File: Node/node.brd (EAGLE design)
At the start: 76.2 x 33.9 mm, 121 parts, among them J1 U.FL, J2 USBSMD, J5 CORTEX_DEBUGPTH, SW2 SPST_TACT-KMR2, U1 MCP73871, U2 DW1000-I, U3 TPS61090RSAR, U4 ATSAMD21G-A, U5 LSM303C, U6 LM3880, X2 332-02, X3 32.768

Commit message: Part modifications, added part numbers to all parts (except resistors and capicators). Library consolidation.
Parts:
- B2: device microbuilder:JSTPH2 -> MainLib:JSTPH2
- C1, C2, C44: device microbuilder:0603-NO -> microbuilder:0603
- C18: value 1p2 -> 1.2pF
- C32: device SparkFun-Passives:0805 -> SparkFun-Capacitors:0603-CAP
- C33: value 100uF/6V - https://www.digikey.com/product-detail/en/avx-corporation/F930G107MBA/478-8135-1-ND/4005827 -> 100uF/6V
- C43: device microbuilder:0805-NO -> SparkFun-Passives:0805
- CHRG, DONE: device microbuilder:CHIPLED_0805_NOOUTLINE -> MainLib:CHIPLED_0805_NOOUTLINE
- D13: value RED -> ORANGE; device microbuilder:CHIPLED_0805_NOOUTLINE -> MainLib:CHIPLED_0805_NOOUTLINE
- J1: device adafruit:U.FL -> MainLib:U.FL
- J2: device SparkFun-Connectors:USB-MINIB -> MainLib:USB-MINIB
- L1, L2: device Wurth_Elektronik_Passive_rev15e:WE-CBA_0402(W=2.2) -> MainLib:WE-CBA_0402(W=2.2)
- L3: value NR8040T6R8N -> 6.8uH, 2A
- PWR, TXUART: value GREEN -> RED; device microbuilder:CHIPLED_0805_NOOUTLINE -> MainLib:CHIPLED_0805_NOOUTLINE
- R1, R2, R3: value 100 -> 470
- R32, R34: value 47K -> 10K
- RV1, RV2, RV3: value WE-VE_0603_REFLOW -> SUPPRESSOR-USB_0603_REFLOW; device Wurth_Elektronik_Passive_rev15e:WESURGE_0603_REFLOW -> MainLib:WESURGE_0603_REFLOW
- RX, RXOK, SFD, TX: device SparkFun-LED:LED-0603 -> MainLib:CHIPLED_0603_NOOUTLINE
- RXUART: value RED -> GREEN; device microbuilder:CHIPLED_0805_NOOUTLINE -> MainLib:CHIPLED_0805_NOOUTLINE
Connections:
- net VCC-ISO: now also R32.2
- net VLIPO: no longer R32.2
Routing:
- net VLIPO: track 12.2 -> 5.38 mm
- net VCC-ISO: track 45.8 -> 50.8 mm

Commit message: Resistor documentation
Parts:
- C1, C2, C44: device microbuilder:0603 -> SparkFun-Capacitors:0603-CAP
- C17, C22, C43, C6: device SparkFun-Passives:0805 -> SparkFun-Capacitors:0603-CAP
- R8, R9: value 10k -> 10K
- renumbered RXUART to UARTRX, TXUART to UARTTX

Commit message: Prep to move to a new power regulator, as previous one is only boost
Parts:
- added C36: 1uF, SparkFun-Capacitors:0603-CAP
- added SJ4, SJ5: (no value), jumper:SJ
- added U$12: 3.3V, MainLib:10-VFDFNEXPOSEDPAD
- R15, R16, R22: value 1K -> 470
- R28: value 68 -> 100K
- RT2: value 15K -> 10K
- renumbered THERM to RT2
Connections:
- new net N$19: C36.2, SJ4.1, U6.3
- net 3.3V: now also SJ4.2, SJ5.2; no longer U6.3
- net GND: now also C36.1
- net VDELAY: now also SJ5.1
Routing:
- net N$19: track 0.00 -> 10.7 mm, vias 0 -> 1
- net VDELAY: track 9.38 -> 14.8 mm, vias 0 -> 1
- net SDA: track 49.2 -> 53.3 mm
- net 3.3V: track 52.1 -> 50.1 mm, vias 26 -> 27
- net !CS_MAG: track 2.36 -> 3.33 mm
- net GND: vias 236 -> 237
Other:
- board text added: "Bubble if no C36"
- board text added: "Bubble if no U6"
- board text removed: "Accel / Compass"

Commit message: Initial pass of the new regulator circuit. Passes DRT.
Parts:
- removed R25: 205K, 1%, SparkFun-Resistors:0603-RES
- removed U3: TPS61090RSAR, microbuilder:PVQFN-16
- C30: value 2.2uF -> 15uF
- L3: value 6.8uH, 2A -> 3.3uH; device MainLib:IND_TAIYO_NR8040 -> MainLib:1212IND
- R24: value 1.15M, 1% -> 100
- moved U$12 12.8 mm to (54.9, 20.0), turned to 270 degrees
- moved L3 6.76 mm to (60.2, 23.4), turned to 90 degrees
- moved C30 6.20 mm to (60.2, 20.1)
- moved C32 5.05 mm to (54.6, 16.5)
- moved R24 3.21 mm to (51.8, 16.6), turned to 180 degrees
- moved C22 0.25 mm to (49.9, 20.3)
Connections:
- removed net N$20: L3.1, U3.3, U3.4
- new net N$29: L3.P1, U$12.PX2
- new net N$37: C32.1, R24.1, U$12.PX7, U$12.PX8
- net 3.3V: now also U$12.PX1, U$12.PX10; no longer R24.2, U3.1, U3.15, U3.16
- net GND: now also U$12.PAD@1, U$12.PX3, U$12.PX9; no longer R25.1, U3.10, U3.13, U3.5, U3.6, U3.7, U3.9, U3.P$18, U3.P$19, U3.P$20, U3.P$21, U3.P$22, U3.THERMAL
- net N$23: now also L3.P2, U$12.PX4; no longer R24.1, R25.2, U3.14
- net N$30: now also U$12.PX6; no longer U3.11
- net VCC-ISO: now also R24.2, U$12.PX5; no longer C32.1, L3.2, U3.8
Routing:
- net N$20: track 16.9 -> 0.00 mm
- net GND: track 8.49 -> 16.8 mm, vias 237 -> 249
- net N$23: track 4.88 -> 0.00 mm
- net VCC-ISO: track 50.9 -> 55.2 mm
- net N$37: track 0.00 -> 4.09 mm
- net N$30: track 57.7 -> 59.2 mm
- net !CS_MAG: track 3.33 -> 2.36 mm
- net 3.3V: track 50.1 -> 50.0 mm, vias 27 -> 26
- added copper zone on layer 1, net N$23
- added copper zone on layer 1, net N$29
- removed copper zone on layer 1, net N$20
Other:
- board text added: "ATSAMD21"
- board text added: "Charger"
- board text added: "Regulator"
- board text removed: "C32"
- board text removed: "R24"
- board text removed: "R25"

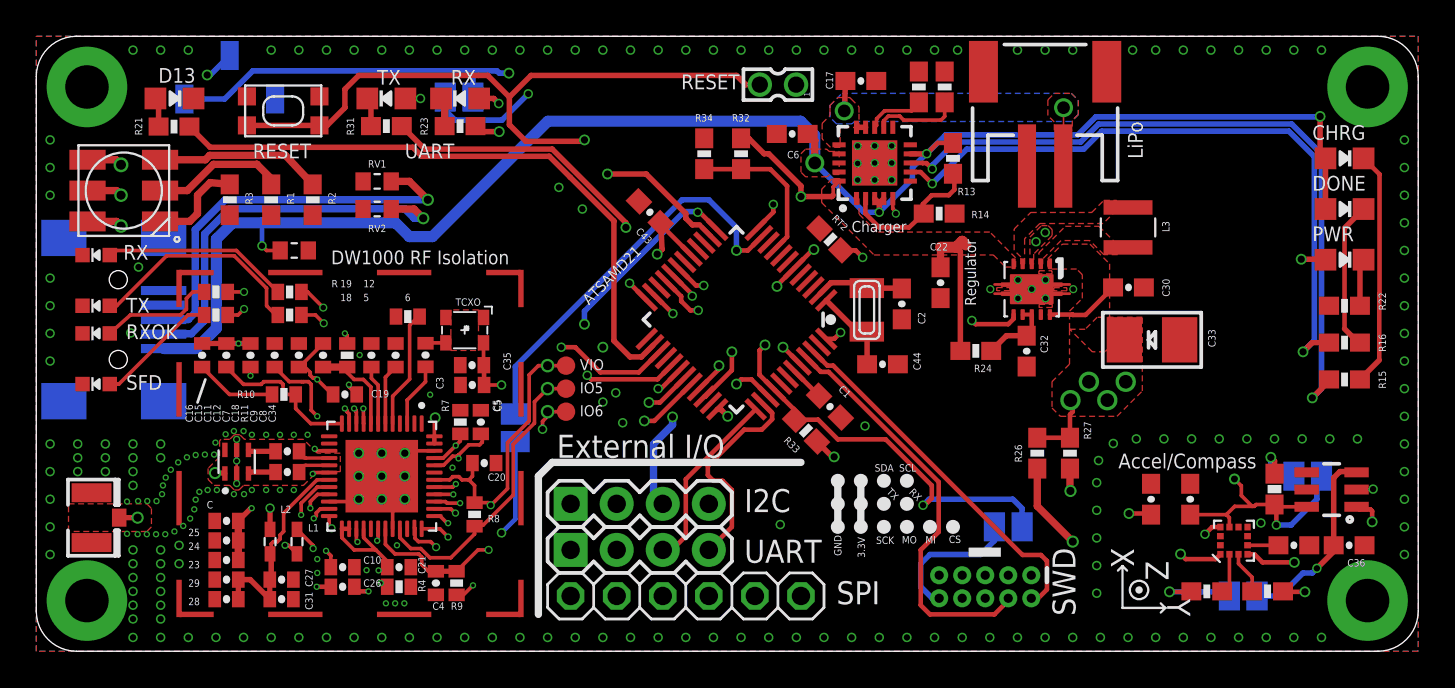
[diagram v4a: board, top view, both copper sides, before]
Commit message: Changes to the regulater schematic
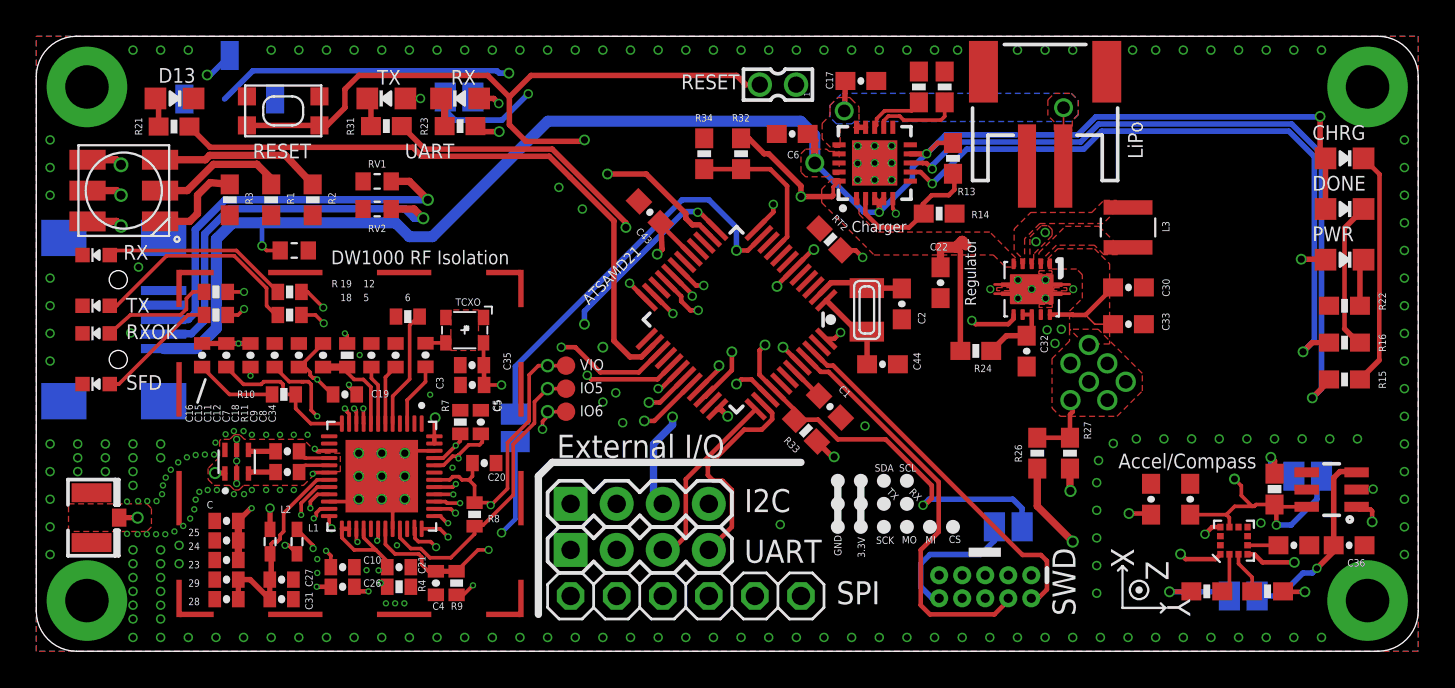
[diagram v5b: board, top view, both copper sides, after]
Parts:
- C30: value 15uF -> 10uF
- C33: value 100uF/6V -> 10uF; device microbuilder:EIA3528-21/B-R -> SparkFun-Capacitors:0603-CAP
- L3: value 3.3uH -> 2.2uH
- moved C33 1.56 mm to (60.2, 18.0), turned to 0 degrees
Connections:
- removed net N$37: C32.1, R24.1, U$12.PX7, U$12.PX8
- new net N$20: C30.1, C33.1, U$12.PX1, U$12.PX10
- new net N$34: C32.1, PWR_SW.P$3, R24.1, SJ2.1, U$12.PX7, U$12.PX8
- net 3.3V: no longer C30.1, C33.+, U$12.PX1, U$12.PX10
- net GND: now also C33.2; no longer C33.-
- net VCC-ISO: no longer PWR_SW.P$3, SJ2.1
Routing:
- net N$20: track 0.00 -> 5.85 mm
- net 3.3V: track 50.0 -> 45.9 mm, vias 26 -> 29
- net N$37: track 4.09 -> 0.00 mm
- net N$34: track 0.00 -> 4.09 mm
- net VCC-ISO: track 55.2 -> 51.6 mm
- net GND: vias 249 -> 252
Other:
- board text removed: "C33"

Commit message: Added RFM69HCW slot for possible use for base-station communications. Routed external SPI slot to SERCOM 2 Alt so the ATSAMD21 can be used as an SPI slave for the RPi (to gather data from the network for processing)
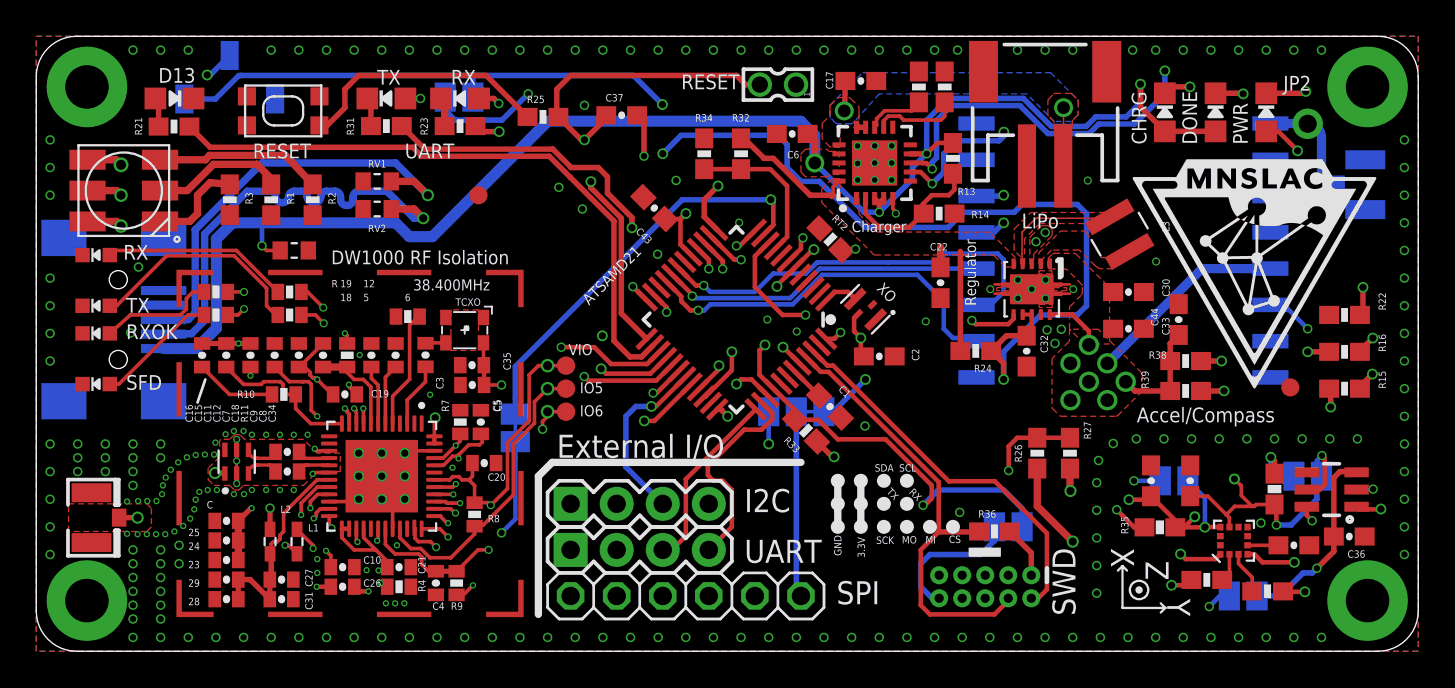
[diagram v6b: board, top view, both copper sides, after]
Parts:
- removed X3: 32.768, adafruit2:XTAL3215
- added C37: 0.1uF, SparkFun-Capacitors:0603-CAP
- added FID3, FID4: FIDUCIAL"", microbuilder:FIDUCIAL_1MM
- added J3: U.FL, MainLib:U.FL
- added JP2: (no value), microbuilder:1X01_ROUND
- added R25: 330, SparkFun-Resistors:0603-RES
- added R35: 100K, SparkFun-Passives:0603-RES
- added R36: 1K, SparkFun-Resistors:0603-RES
- added R38, R39: 100K, SparkFun-Resistors:0603-RES
- added SJ6: (no value), jumper:SJ
- added SJ7: (no value), jumper:SJ_2
- added TP4: VDD_TP, SparkFun-Passives:TP_15TH
- added U$11: 32.768kHz, MainLib:MEMS4-SMD
- added U$14: MNSLAC0.25, MainLib:MNSLAC-0.25
- added U3: RFM69HCW, microbuilder:RFMHCW_SMT
- C2: value 22pF -> 0.1uF
- C25, C29, C35: value 100nF -> 0.1uF
- C44: value 22pF -> 10uF
- R33: value 10K -> 2K
- moved C44 16.5 mm to (63.0, 18.3), turned to 90 degrees
- moved CHRG 10.2 mm to (62.2, 29.7), turned to 0 degrees
- moved PWR 9.20 mm to (67.8, 29.7), turned to 0 degrees
- moved DONE 8.89 mm to (65.0, 29.7), turned to 0 degrees
- moved U$1 3.42 mm to (66.6, 28.2)
- moved C2 3.15 mm to (46.5, 16.3), turned to 0 degrees
- moved C39 1.02 mm to (63.6, 9.40)
- moved C41 1.02 mm to (61.5, 9.40)
- moved R29 0.63 mm to (64.5, 3.93)
- moved L3 0.59 mm to (59.7, 23.0), turned to 120 degrees
- moved R15 0.51 mm to (72.1, 14.5)
- moved R16 0.51 mm to (72.1, 16.5)
- moved R22 0.51 mm to (72.1, 18.5)
- moved C36 0.48 mm to (72.4, 6.32)
- moved C43 0.34 mm to (34.1, 24.4)
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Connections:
- net A5 renamed !RFTCS
- removed net !RST: SJ1.2, U2.27
- removed net A1: U4.7
- removed net A4: U4.10
- removed net D0: U4.16
- removed net D1: U4.15
- removed net D11: U4.25
- removed net D12: U4.28
- removed net DWRST: SJ1.1, U4.11
- removed net VDELAY: C39.1, R28.2, SJ5.1, TP3.P$1, U5.9, U6.6
- new net !DWRST: SJ1.1, SJ1.2, U2.27, U4.11
- new net !EXTCSCOM: SJ7.2, SJ7.3, SPI.6, U4.13
- new net !RFMCS: R38.1, U3.13P
- new net !RFMRST: R39.1, U3.14P, U4.10
- new net LSMDELAY: C39.1, R28.2, SJ5.1, TP3.P$1, U5.9, U6.5
- new net LSMVDDIO: C41.1, R26.2, R27.2, R29.1, R30.1, R35.2, SJ6.1, TP4.P$1, U5.10, U6.6
- new net MISO_EXT: SPI.5, U4.14
- new net MOSI_EXT: SPI.4, U4.15
- new net RFMIQR: U3.6P, U4.7
- new net SCK_EXT: SPI.3, U4.16
- net !EXTCS: now also SJ7.1; no longer SPI.6
- net !RESET: now also C37.1, R25.2; no longer SW2.1, SW2.3
- net 3.3V: now also C2.1, C30.1, C33.1, C37.2, C44.1, R35.1, R36.2, R38.2, R39.2, SJ6.2, U$11.P4, U$12.PX1, U$12.PX10, U3.5P; no longer C41.1, R26.2, R27.2, R29.1, R30.1, U5.10
- net EXTON: now also U4.28; no longer U4.13
- net GND: now also J3.1, J3.2, U$11.P2, U3.16P, U3.2P, U3.9P
- net MISO: now also U3.10P; no longer SPI.5
- net MOSI: now also U3.11P; no longer SPI.4
- net N$20: now also R25.1, SW2.3; no longer C30.1, C33.1, U$12.PX1, U$12.PX10
- net N$35: now also U$11.P3, U4.1; no longer C2.1, U4.2, X3.P$1
- net N$36: now also J3.3, JP2.1, U3.1P; no longer C44.1, U4.1, X3.P$2
- net RED: now also U4.25; no longer U4.14
- net SCK: now also U3.12P; no longer SPI.3
- net SWCLK: now also R36.1
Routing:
- net N$34: track 4.09 -> 77.0 mm, vias 0 -> 3
- net !RFMRST: track 0.00 -> 46.6 mm, vias 0 -> 3
- net !DWRST: track 0.00 -> 44.2 mm, vias 0 -> 3
- net RFMIQR: track 0.00 -> 40.0 mm, vias 0 -> 2
- net LSMVDDIO: track 0.00 -> 39.6 mm, vias 0 -> 6
- net VCC-ISO: track 51.6 -> 14.0 mm, vias 2 -> 0
- net !EXTCSCOM: track 0.00 -> 34.3 mm, vias 0 -> 2
- net MISO_EXT: track 0.00 -> 24.6 mm, vias 0 -> 1
- net !RFMCS: track 0.00 -> 23.4 mm, vias 0 -> 2
- net DWRST: track 22.3 -> 0.00 mm, vias 1 -> 0
- net SCK_EXT: track 0.00 -> 22.2 mm, vias 0 -> 1
- net MOSI_EXT: track 0.00 -> 22.1 mm, vias 0 -> 1
- net 3.3V: track 45.9 -> 66.9 mm, vias 29 -> 30
- net !RESET: track 80.0 -> 60.2 mm
- net !RST: track 18.1 -> 0.00 mm, vias 2 -> 0
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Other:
- board text added: "Cut to disconnect SAMD21 from DW1000 !DWRST"
- board text added: "D7"
- board text added: "MNSLAC Node"
- board text added: "SERCOM"
- board text added: "XO"
- board text removed: "Bubble to connect SAMD21 to DW1000 !RST"
- board text removed: "C2"
- board text removed: "C44"
- board text removed: "MNSLAC Node ToF Distance, Attitude, Heading, Data Transfer"

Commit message: Refinement, checking components, etc.
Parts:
- added U$15, U$23: RFLOGO0.1, MainLib:RFLOGO-0.1
- R12, R18, R19, R5: device SparkFun-Passives:0402-RES -> SparkFun-Resistors:0603-RES
- R17: value 2.0K -> 1K
- R25: value 330 -> 470
- R33: value 2K -> 4.7K
- R4: value 10K -> 16K
- R7: value 100K -> 16K
- R8, R9: value 10K -> UNUSED-10K
- moved J3 0.99 mm to (72.3, 25.7), turned to 90 degrees
- moved R19 0.19 mm to (9.95, 20.0)
- moved R12 0.18 mm to (14.0, 20.0)
- moved C19 0.08 mm to (17.0, 14.2)
- turned RV3 to 180 degrees
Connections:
- removed net GPIO4: U2.34
- removed net N$27: U2.4
- removed net SYNC: U2.29
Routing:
- net 3.3V: track 66.9 -> 78.5 mm, vias 30 -> 46
- net D-: track 46.8 -> 43.3 mm
- net D+: track 47.4 -> 43.9 mm
- net VBUS: track 85.7 -> 84.3 mm
- net N$36: track 6.11 -> 5.01 mm
- net GPIO0: track 24.0 -> 24.5 mm
- net GND: vias 262 -> 269
- added copper zone on layer 2, net 3.3V
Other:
- board text added: "C39"
- board text added: "C41"
- board text added: "Heatsink"
- board text added: "R17"
- board text added: "R20"
- board text added: "R28"
- board text added: "R29"
- board text added: "R30"
- board text added: "R6"
- board text removed: "6"

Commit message: Detailed changes, small stuff. Checking everything over. Switched to the new SAMD21 package.
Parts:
- removed RV1, RV2, RV3: SUPPRESSOR-USB_0603_REFLOW, MainLib:WESURGE_0603_REFLOW
- added BOTTOM-LOGO: MNSLAC0.25, MainLib:MNSLAC-0.25
- added J4: (no value), SparkFun-Connectors:1X02
- added U$25: ESD7L, MainLib:SOT-723
- U$1: value MNSLAC0.25 -> FOUR_LAYER_WARNING; device MainLib:MNSLAC-0.25 -> SparkFun-Aesthetics:FOUR_LAYER_WARNING
- U2: device MainLib:QFN40P600X600X90-49N -> MainLib:QFN40P600X600X90-49T410
- U4: value ATSAMD21G-A -> SAMD21G18A-AUTTQFN48; device samd21:TQFP-48 -> MainLib:QFP50P900X900X120-48
- moved U$1 36.6 mm to (49.3, -4.06), flipped to the top
- moved TP2 0.51 mm to (29.2, 12.7)
- moved R9 0.48 mm to (23.7, 3.76)
- moved C44 0.45 mm to (63.0, 18.7)
- moved C25 0.44 mm to (10.7, 7.58)
- moved C32 0.43 mm to (54.6, 16.1)
- moved C24 0.37 mm to (10.7, 6.41)
- moved U$11 0.34 mm to (45.8, 19.2)
- moved C23 0.30 mm to (10.7, 5.25)
- moved R10 0.25 mm to (13.7, 13.9)
- moved TP1 0.25 mm to (29.2, 14.2)
- moved C36 0.20 mm to (72.6, 6.32)
- moved C5 0.18 mm to (24.7, 12.6)
- moved C26 0.18 mm to (16.9, 3.38)
- moved R4 0.18 mm to (20.0, 3.38)
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- renumbered U$14 to TOP-LOGO
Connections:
- net D+: now also U$25.P$2; no longer RV1.1
- net D-: now also U$25.P$1; no longer RV2.1
- net GND: now also J4.1, U$25.P$3; no longer RV1.2, RV2.2, RV3.2
- net VBUS: no longer RV3.1
- net VLIPO: now also J4.2
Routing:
- net VBUS: track 84.3 -> 79.7 mm, vias 5 -> 4
- net D-: track 43.3 -> 40.8 mm
- net D+: track 43.9 -> 41.5 mm
- net !RESET: track 60.2 -> 57.9 mm
- net GRN: track 39.0 -> 37.3 mm
- net VLIPO: track 5.38 -> 6.96 mm, vias 2 -> 1
- net GND: track 16.8 -> 18.1 mm, vias 269 -> 270
- net 3.3V: track 78.5 -> 79.4 mm
- net GPIO6: track 21.1 -> 21.9 mm, vias 4 -> 3
- net LSMVDDIO: track 39.6 -> 40.3 mm
- net N$4: track 5.33 -> 4.69 mm
- net N$8: track 8.17 -> 7.62 mm
- added copper zone on layer 15, net VLIPO
- removed copper zone on layer 16, net VLIPO
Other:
- board text added: "HS1"
- board text added: "HS2"
- board text added: "HS3"
- board text added: "HS4"
- board text added: "HS5"
- board text added: "MNSLAC Node PCB"
- board text removed: "RV1"
- board text removed: "RV2"
